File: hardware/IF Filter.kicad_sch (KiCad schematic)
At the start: 10 parts

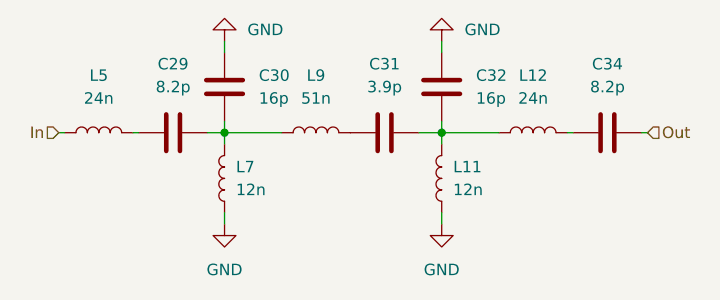
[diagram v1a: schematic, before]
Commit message: Update FEM hardware design for production version
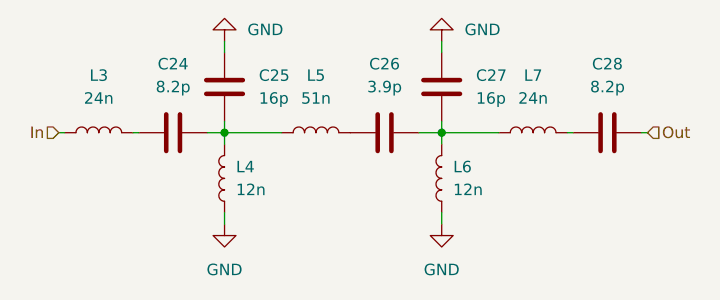
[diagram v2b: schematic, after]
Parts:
- renumbered C29 to C24, C30 to C25, C31 to C26, C32 to C27, C34 to C28, L5 to L3, L7 to L4, L9 to L5, L11 to L6, L12 to L7
